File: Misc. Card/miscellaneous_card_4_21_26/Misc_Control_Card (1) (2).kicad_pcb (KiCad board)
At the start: 4 copper layers, 99.9 x 62 mm, 44 parts, among them IC2 Port 1 Conn_01x02, IC2 Port 2 Conn_01x02, IC2 Port 3 Conn_01x02, J1 Conn_01x03_Pin, J2 Conn_01x02, J3 Conn_01x02, J4 Conn_01x02, J5 Conn_01x02, J7 Screw_Terminal_01x02, J8 Conn_01x03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

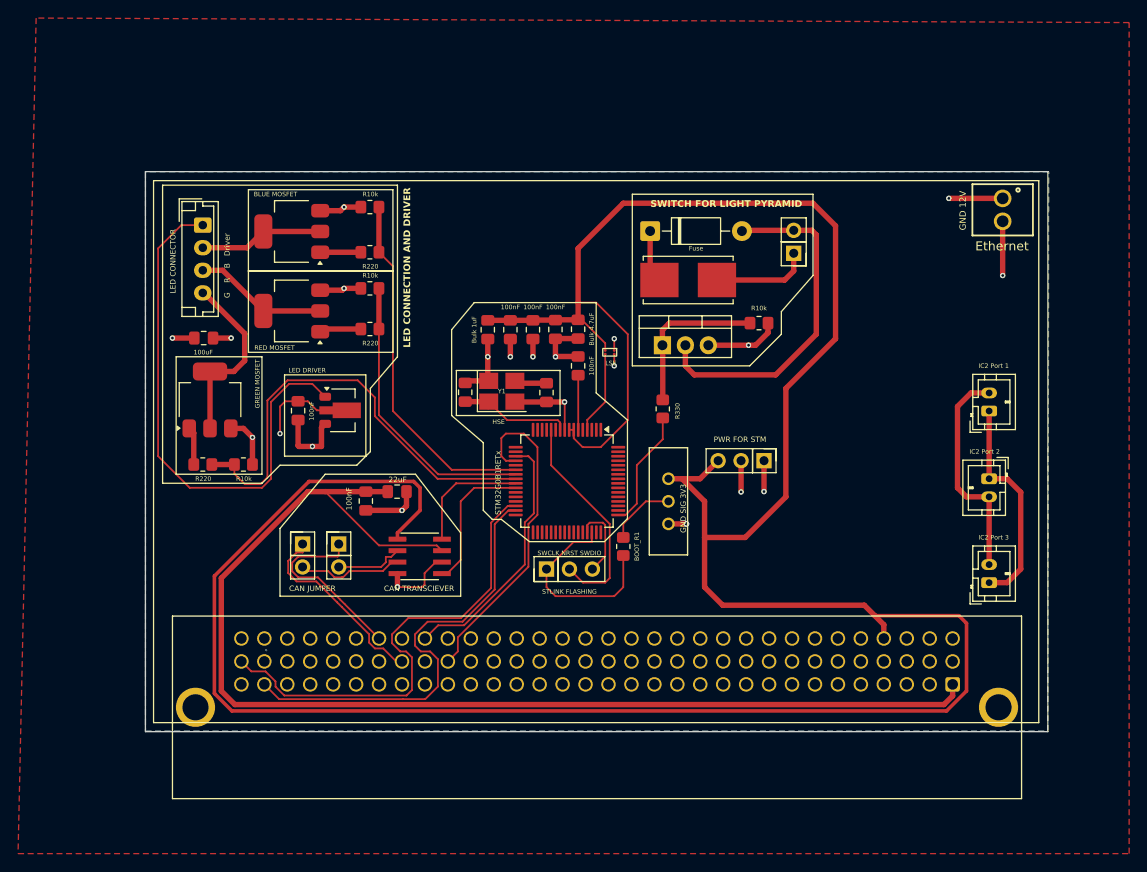
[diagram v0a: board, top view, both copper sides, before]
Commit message: Added CAN Impedance Matching
Misc Card
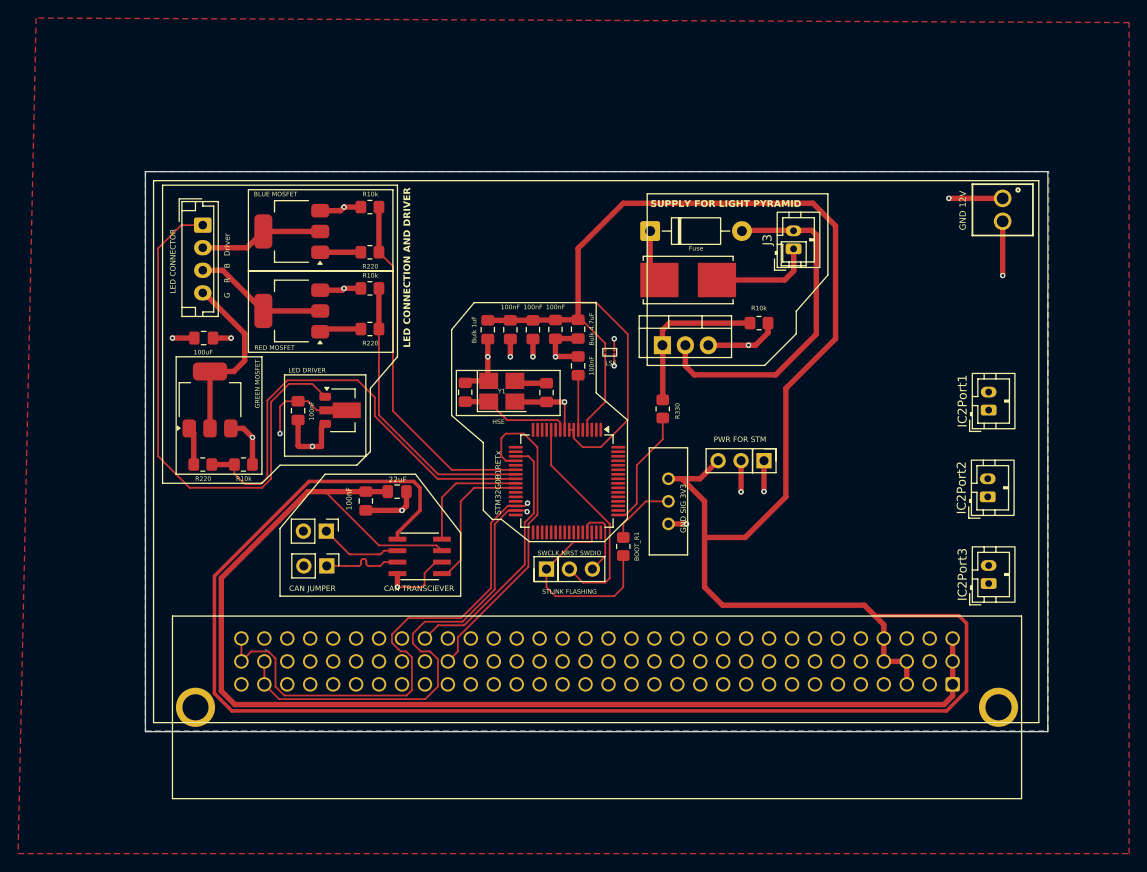
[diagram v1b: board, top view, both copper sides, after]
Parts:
- removed IC2 Port 1: Conn_01x02, Connector_JST:JST_PH_B2B-PH-K_1x02_P2.00mm_Vertical
- removed IC2 Port 2: Conn_01x02, Connector_JST:JST_PH_B2B-PH-K_1x02_P2.00mm_Vertical
- removed IC2 Port 3: Conn_01x02, Connector_JST:JST_PH_B2B-PH-K_1x02_P2.00mm_Vertical
- added IC2Port1: Conn_01x02, Connector_JST:JST_PH_B2B-PH-K_1x02_P2.00mm_Vertical, F.Cu at (243.4, 75.4)
- added IC2Port2: Conn_01x02, Connector_JST:JST_PH_B2B-PH-K_1x02_P2.00mm_Vertical, F.Cu at (243.3, 85.0)
- added IC2Port3: Conn_01x02, Connector_JST:JST_PH_B2B-PH-K_1x02_P2.00mm_Vertical, F.Cu at (243.4, 94.6)
- J3: footprint Connector_PinHeader_2.54mm:PinHeader_1x02_P2.54mm_Vertical -> Connector_JST:JST_PH_B2B-PH-K_1x02_P2.00mm_Vertical
- moved J4 3.61 mm to (170.2, 92.7), turned to -90 degrees
- moved J5 1.98 mm to (170.1, 88.8), turned to -90 degrees
- moved J3 0.49 mm to (221.8, 57.5), turned to 90 degrees
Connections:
- J4 pad 1: CAN+ -> CAN_misc+
- J5 pad 1: CAN- -> CAN_misc-
- U6 pad 6: CAN- -> CAN_misc-
- U6 pad 7: CAN+ -> CAN_misc+
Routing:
- net SCL_IN: track 52.3 -> 143.1 mm, vias 0 -> 1
- net SDA_IN: track 49.0 -> 124.1 mm, vias 0 -> 1
- net IC2_JETSON-: track 24.5 -> 0.00 mm
- net IC2_JETSON+: track 24.2 -> 0.00 mm
- net CAN+: track 36.5 -> 22.5 mm
- net CAN_misc+: track 0.00 -> 12.4 mm
- net CAN_misc-: track 0.00 -> 11.2 mm
- net CAN-: track 30.1 -> 21.8 mm
- net 3.3v: track 316.8 -> 324.5 mm
- net 5V: track 133.8 -> 138.9 mm
- net GND: vias 21 -> 19
- added copper zone on F.Cu, net +12V
- removed copper zone on F.Cu, net (none)
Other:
- board text added: "SUPPLY FOR LIGHT PYRAMID"
- board text removed: "${REFERENCE}"
- board text removed: "Ethernet"
- board text removed: "SWITCH FOR LIGHT PYRAMID"

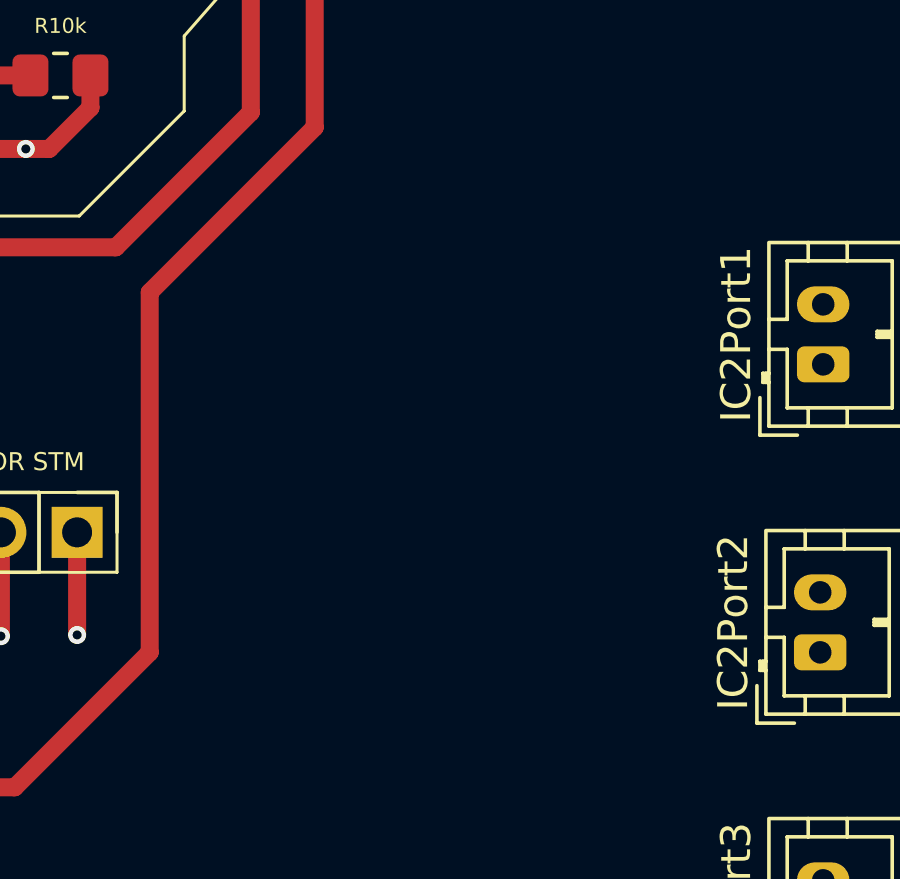
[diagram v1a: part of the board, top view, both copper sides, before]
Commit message: Added Silkscreen & Backplane Integration
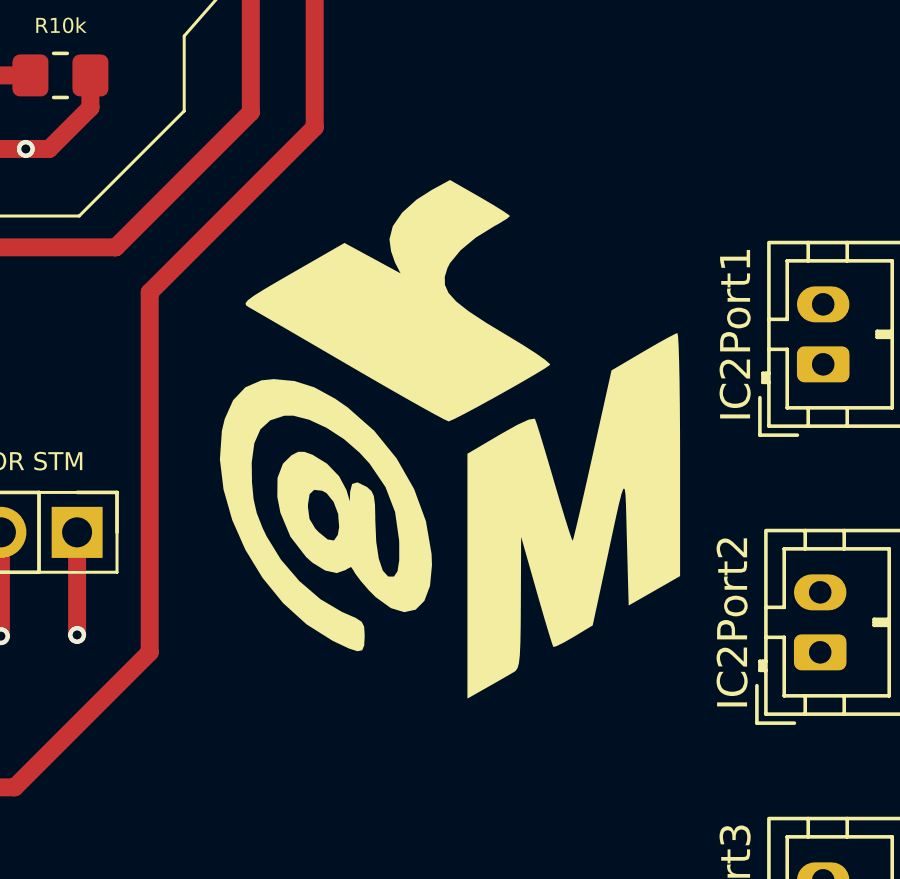
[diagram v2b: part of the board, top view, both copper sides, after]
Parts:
- added G***: LOGO, LOGO, F.Cu at (231.0, 77.9)
- added G***: LOGO, LOGO, B.Cu at (182.2, 63.0)
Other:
- board text added: "Misc Card 2026"
